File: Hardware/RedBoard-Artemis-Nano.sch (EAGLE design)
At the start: 67 parts, among them J10 USB Female Type C Connector, J11 CORTEX_DEBUG, U1 ARTEMIS_MODULESMD, U2 MCP73831, U3 3.3V, U6 CH340E_MSOP10, Y2 32.768kHz

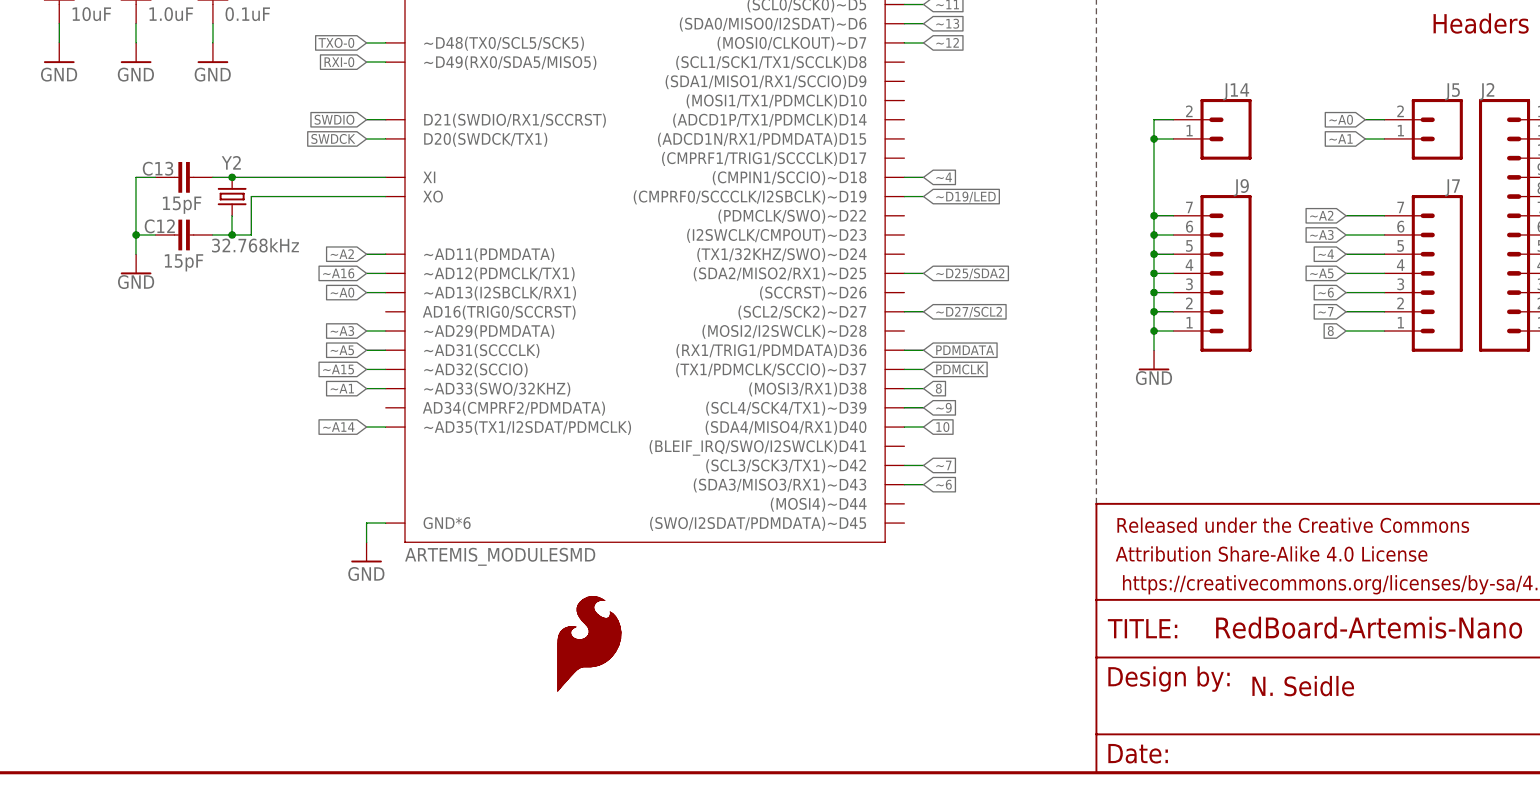
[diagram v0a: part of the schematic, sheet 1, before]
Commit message: Changed silk around PSWC PTH.
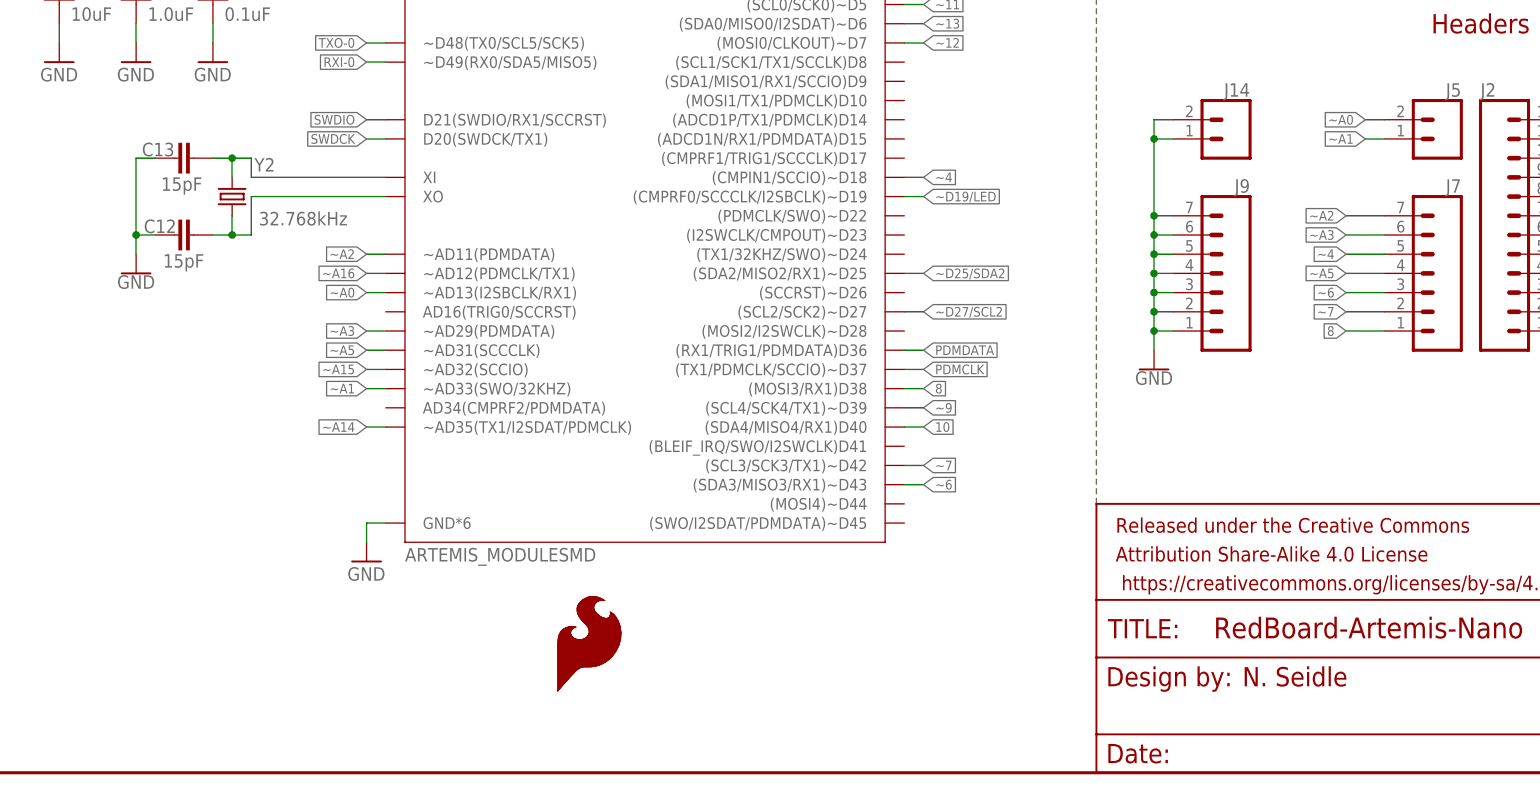
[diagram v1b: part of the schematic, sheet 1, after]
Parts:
- J11: device SparkFun-Connectors:CORTEX_DEBUG_MINIMUM_PTH_NS -> SparkFun-Connectors:CORTEX_JTAG_DEBUG_MINIMUM_PTH_NS
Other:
- moved on the sheet: C13
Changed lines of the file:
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@@
 <?xml version="1.0" encoding="utf-8"?>
 <!DOCTYPE eagle SYSTEM "eagle.dtd">
-<eagle version="9.4.0">
+<eagle version="9.4.2">
 <drawing>
 <settings>
@@
 <part name="TP1" library="SparkFun-Connectors" deviceset="TEST-POINT" device="3X5" value=""/>
 <part name="TP2" library="SparkFun-Connectors" deviceset="TEST-POINT" device="3X5" value=""/>
-<part name="J11" library="SparkFun-Connectors" deviceset="CORTEX_DEBUG_MINIMUM" device="_PTH_NS" value="CORTEX_DEBUG"/>
+<part name="J11" library="SparkFun-Connectors" deviceset="CORTEX_JTAG_DEBUG_MINIMUM" device="_PTH_NS" value="CORTEX_DEBUG"/>
 <part name="SUPPLY1" library="SparkFun-PowerSymbols" deviceset="3.3V" device=""/>
 <part name="SUPPLY2" library="SparkFun-PowerSymbols" deviceset="3.3V" device=""/>
@@
 <wire x1="147.32" y1="104.14" x2="147.32" y2="137.16" width="0.1524" layer="97" style="longdash"/>
 <text x="238.76" y="7.62" size="2.54" layer="94">v10</text>
-<text x="167.64" y="10.16" size="2.54" layer="94">N. Seidle</text>
+<text x="166.624" y="11.43" size="2.54" layer="94">N. Seidle</text>
 <wire x1="147.32" y1="104.14" x2="248.92" y2="104.14" width="0.1524" layer="97" style="longdash"/>
 <text x="198.374" y="133.096" size="2.54" layer="94" ratio="15" align="center">SWD Program/Debug Interface</text>
@@
 </instance>
 <instance part="Y2" gate="G$1" x="33.02" y="76.2" smashed="yes" rot="R270">
-<attribute name="NAME" x="33.02" y="79.756" size="1.778" layer="95" font="vector" align="bottom-center"/>
-<attribute name="VALUE" x="36.068" y="70.612" size="1.778" layer="96" font="vector" align="top-center"/>
+<attribute name="NAME" x="37.338" y="79.502" size="1.778" layer="95" font="vector" align="bottom-center"/>
+<attribute name="VALUE" x="42.418" y="74.168" size="1.778" layer="96" font="vector" align="top-center"/>
 </instance>
 <instance part="C12" gate="G$1" x="27.94" y="71.12" smashed="yes" rot="R90">
@@
 <attribute name="VALUE" x="23.876" y="68.58" size="1.778" layer="96" font="vector" rot="MR180"/>
 </instance>
-<instance part="C13" gate="G$1" x="27.94" y="78.74" smashed="yes" rot="R90">
-<attribute name="NAME" x="21.082" y="78.994" size="1.778" layer="95" font="vector"/>
-<attribute name="VALUE" x="23.622" y="76.2" size="1.778" layer="96" font="vector" rot="MR180"/>
+<instance part="C13" gate="G$1" x="27.94" y="81.28" smashed="yes" rot="R90">
+<attribute name="NAME" x="21.082" y="81.534" size="1.778" layer="95" font="vector"/>
+<attribute name="VALUE" x="23.622" y="78.74" size="1.778" layer="96" font="vector" rot="MR180"/>
 </instance>
 <instance part="GND35" gate="1" x="20.32" y="66.04" smashed="yes">
@@
 <segment>
 <pinref part="C13" gate="G$1" pin="1"/>
-<wire x1="22.86" y1="78.74" x2="20.32" y2="78.74" width="0.1524" layer="91"/>
-<wire x1="20.32" y1="78.74" x2="20.32" y2="71.12" width="0.1524" layer="91"/>
+<wire x1="22.86" y1="81.28" x2="20.32" y2="81.28" width="0.1524" layer="91"/>
+<wire x1="20.32" y1="81.28" x2="20.32" y2="71.12" width="0.1524" layer="91"/>
 <pinref part="GND35" gate="1" pin="GND"/>
 <pinref part="C12" gate="G$1" pin="1"/>
@@
 <segment>
 <pinref part="Y2" gate="G$1" pin="1"/>
-<wire x1="53.34" y1="78.74" x2="33.02" y2="78.74" width="0.1524" layer="91"/>
+<wire x1="53.34" y1="78.74" x2="35.56" y2="78.74" width="0.1524" layer="91"/>
 <pinref part="C13" gate="G$1" pin="2"/>
-<wire x1="33.02" y1="78.74" x2="30.48" y2="78.74" width="0.1524" layer="91"/>
-<junction x="33.02" y="78.74"/>
 <pinref part="U1" gate="U1" pin="XI"/>
-</segment>
-</net>
+<wire x1="35.56" y1="78.74" x2="35.56" y2="81.28" width="0.1524" layer="91"/>
+<wire x1="35.56" y1="81.28" x2="33.02" y2="81.28" width="0.1524" layer="91"/>
+<wire x1="33.02" y1="81.28" x2="30.48" y2="81.28" width="0.1524" layer="91"/>
+<wire x1="33.02" y1="78.74" x2="33.02" y2="81.28" width="0.1524" layer="91"/>
+<junction x="33.02" y="81.28"/>
+</segment>
+</net>

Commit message: Adding production panels
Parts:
- U1: device Testing:ARTEMIS_MODULESMD -> SparkFun-IC-Microcontroller:ARTEMIS_MODULESMD
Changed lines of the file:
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@@
 <part name="GND1" library="SparkFun-PowerSymbols" deviceset="GND" device=""/>
 <part name="SUPPLY12" library="SparkFun-PowerSymbols" deviceset="3.3V" device=""/>
-<part name="U1" library="Testing" deviceset="ARTEMIS_MODULE" device="SMD"/>
+<part name="U1" library="SparkFun-IC-Microcontroller" deviceset="ARTEMIS_MODULE" device="SMD"/>
 <part name="J4" library="SparkFun-Connectors" deviceset="CONN_02" device="1X02_NO_SILK"/>
 <part name="R1" library="SparkFun-Resistors" deviceset="10KOHM" device="-0603-1/10W-1%" value="10k"/>

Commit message: Add OSHW logo
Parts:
- added LOGO2: OSHW-LOGONO_SILK, SparkFun-Aesthetics:OSHW-LOGONO_SILK
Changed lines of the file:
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@@
 <grid distance="0.1" unitdist="inch" unit="inch" style="lines" multiple="1" display="no" altdistance="0.01" altunitdist="inch" altunit="inch"/>
 <layers>
-<layer number="1" name="Top" color="4" fill="1" visible="no" active="no"/>
-<layer number="2" name="Route2" color="16" fill="3" visible="no" active="no"/>
-<layer number="3" name="Route3" color="4" fill="3" visible="no" active="no"/>
-<layer number="4" name="Route4" color="1" fill="4" visible="no" active="no"/>
-<layer number="5" name="Route5" color="4" fill="4" visible="no" active="no"/>
-<layer number="6" name="Route6" color="1" fill="8" visible="no" active="no"/>
-<layer number="7" name="Route7" color="4" fill="8" visible="no" active="no"/>
-<layer number="8" name="Route8" color="1" fill="2" visible="no" active="no"/>
-<layer number="9" name="Route9" color="4" fill="2" visible="no" active="no"/>
-<layer number="10" name="Route10" color="1" fill="7" visible="no" active="no"/>
-<layer number="11" name="Route11" color="4" fill="7" visible="no" active="no"/>
-<layer number="12" name="Route12" color="1" fill="5" visible="no" active="no"/>
-<layer number="13" name="Route13" color="4" fill="5" visible="no" active="no"/>
-<layer number="14" name="Route14" color="1" fill="6" visible="no" active="no"/>
-<layer number="15" name="Route15" color="23" fill="6" visible="no" active="no"/>
-<layer number="16" name="Bottom" color="1" fill="1" visible="no" active="no"/>
-<layer number="17" name="Pads" color="2" fill="1" visible="no" active="no"/>
-<layer number="18" name="Vias" color="2" fill="1" visible="no" active="no"/>
-<layer number="19" name="Unrouted" color="6" fill="1" visible="no" active="no"/>
-<layer number="20" name="Dimension" color="24" fill="1" visible="no" active="no"/>
-<layer number="21" name="tPlace" color="16" fill="1" visible="no" active="no"/>
-<layer number="22" name="bPlace" color="14" fill="1" visible="no" active="no"/>
-<layer number="23" name="tOrigins" color="15" fill="1" visible="no" active="no"/>
-<layer number="24" name="bOrigins" color="15" fill="1" visible="no" active="no"/>
-<layer number="25" name="tNames" color="7" fill="1" visible="no" active="no"/>
-<layer number="26" name="bNames" color="7" fill="1" visible="no" active="no"/>
-<layer number="27" name="tValues" color="7" fill="1" visible="no" active="no"/>
-<layer number="28" name="bValues" color="7" fill="1" visible="no" active="no"/>
+<layer number="1" name="Top" color="4" fill="1" visible="yes" active="no"/>
+<layer number="2" name="Route2" color="16" fill="3" visible="yes" active="no"/>
+<layer number="3" name="Route3" color="4" fill="3" visible="yes" active="no"/>
+<layer number="4" name="Route4" color="1" fill="4" visible="yes" active="no"/>
+<layer number="5" name="Route5" color="4" fill="4" visible="yes" active="no"/>
+<layer number="6" name="Route6" color="1" fill="8" visible="yes" active="no"/>
+<layer number="7" name="Route7" color="4" fill="8" visible="yes" active="no"/>
+<layer number="8" name="Route8" color="1" fill="2" visible="yes" active="no"/>
+<layer number="9" name="Route9" color="4" fill="2" visible="yes" active="no"/>
+<layer number="10" name="Route10" color="1" fill="7" visible="yes" active="no"/>
+<layer number="11" name="Route11" color="4" fill="7" visible="yes" active="no"/>
+<layer number="12" name="Route12" color="1" fill="5" visible="yes" active="no"/>
+<layer number="13" name="Route13" color="4" fill="5" visible="yes" active="no"/>
+<layer number="14" name="Route14" color="1" fill="6" visible="yes" active="no"/>
+<layer number="15" name="Route15" color="23" fill="6" visible="yes" active="no"/>
+<layer number="16" name="Bottom" color="1" fill="1" visible="yes" active="no"/>
+<layer number="17" name="Pads" color="2" fill="1" visible="yes" active="no"/>
+<layer number="18" name="Vias" color="2" fill="1" visible="yes" active="no"/>
+<layer number="19" name="Unrouted" color="6" fill="1" visible="yes" active="no"/>
+<layer number="20" name="Dimension" color="24" fill="1" visible="yes" active="no"/>
+<layer number="21" name="tPlace" color="16" fill="1" visible="yes" active="no"/>
+<layer number="22" name="bPlace" color="14" fill="1" visible="yes" active="no"/>
+<layer number="23" name="tOrigins" color="15" fill="1" visible="yes" active="no"/>
+<layer number="24" name="bOrigins" color="15" fill="1" visible="yes" active="no"/>
+<layer number="25" name="tNames" color="7" fill="1" visible="yes" active="no"/>
+<layer number="26" name="bNames" color="7" fill="1" visible="yes" active="no"/>
+<layer number="27" name="tValues" color="7" fill="1" visible="yes" active="no"/>
+<layer number="28" name="bValues" color="7" fill="1" visible="yes" active="no"/>
 <layer number="29" name="tStop" color="7" fill="3" visible="no" active="no"/>
 <layer number="30" name="bStop" color="7" fill="6" visible="no" active="no"/>
@@
 <layer number="35" name="tGlue" color="7" fill="4" visible="no" active="no"/>
 <layer number="36" name="bGlue" color="7" fill="5" visible="no" active="no"/>
-<layer number="37" name="tTest" color="7" fill="1" visible="no" active="no"/>
-<layer number="38" name="bTest" color="7" fill="1" visible="no" active="no"/>
+<layer number="37" name="tTest" color="7" fill="1" visible="yes" active="no"/>
+<layer number="38" name="bTest" color="7" fill="1" visible="yes" active="no"/>
 <layer number="39" name="tKeepout" color="4" fill="11" visible="no" active="no"/>
 <layer number="40" name="bKeepout" color="1" fill="11" visible="no" active="no"/>
@@
 <layer number="44" name="Drills" color="7" fill="1" visible="no" active="no"/>
 <layer number="45" name="Holes" color="7" fill="1" visible="no" active="no"/>
-<layer number="46" name="Milling" color="3" fill="1" visible="no" active="no"/>
-<layer number="47" name="Measures" color="7" fill="1" visible="no" active="no"/>
-<layer number="48" name="Document" color="7" fill="1" visible="no" active="no"/>
-<layer number="49" name="Reference" color="7" fill="1" visible="no" active="no"/>
-<layer number="50" name="dxf" color="7" fill="1" visible="no" active="no"/>
-<layer number="51" name="tDocu" color="6" fill="1" visible="no" active="no"/>
-<layer number="52" name="bDocu" color="7" fill="1" visible="no" active="no"/>
-<layer number="53" name="tGND_GNDA" color="7" fill="9" visible="no" active="no"/>
-<layer number="54" name="bGND_GNDA" color="1" fill="9" visible="no" active="no"/>
-<layer number="56" name="wert" color="7" fill="1" visible="no" active="no"/>
-<layer number="57" name="tCAD" color="7" fill="1" visible="no" active="no"/>
-<layer number="59" name="tCarbon" color="7" fill="1" visible="no" active="no"/>
-<layer number="60" name="bCarbon" color="7" fill="1" visible="no" active="no"/>
+<layer number="46" name="Milling" color="3" fill="1" visible="yes" active="no"/>
+<layer number="47" name="Measures" color="7" fill="1" visible="yes" active="no"/>
+<layer number="48" name="Document" color="7" fill="1" visible="yes" active="no"/>
+<layer number="49" name="Reference" color="7" fill="1" visible="yes" active="no"/>
+<layer number="50" name="dxf" color="7" fill="1" visible="yes" active="no"/>
+<layer number="51" name="tDocu" color="6" fill="1" visible="yes" active="no"/>
+<layer number="52" name="bDocu" color="7" fill="1" visible="yes" active="no"/>
+<layer number="53" name="tGND_GNDA" color="7" fill="9" visible="yes" active="no"/>
+<layer number="54" name="bGND_GNDA" color="1" fill="9" visible="yes" active="no"/>
+<layer number="56" name="wert" color="7" fill="1" visible="yes" active="no"/>
+<layer number="57" name="tCAD" color="7" fill="1" visible="yes" active="no"/>
+<layer number="59" name="tCarbon" color="7" fill="1" visible="yes" active="no"/>
+<layer number="60" name="bCarbon" color="7" fill="1" visible="yes" active="no"/>
 <layer number="88" name="SimResults" color="9" fill="1" visible="yes" active="yes"/>
 <layer number="89" name="SimProbes" color="9" fill="1" visible="yes" active="yes"/>
@@
 <part name="TP3" library="SparkFun-Connectors" deviceset="TEST-POINT" device="3X5"/>
 <part name="TP4" library="SparkFun-Connectors" deviceset="TEST-POINT" device="3X5"/>
+<part name="LOGO2" library="SparkFun-Aesthetics" deviceset="OSHW-LOGO" device="NO_SILK" value="OSHW-LOGONO_SILK"/>
 </parts>
 <sheets>
@@
 <attribute name="VALUE" x="195.58" y="144.526" size="1.778" layer="96" align="top-center"/>
 </instance>
+<instance part="LOGO2" gate="G$1" x="132.08" y="12.7" smashed="yes"/>
 </instances>
 <busses>
